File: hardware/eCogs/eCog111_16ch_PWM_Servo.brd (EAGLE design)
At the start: 47.5 x 28 mm, 4 parts

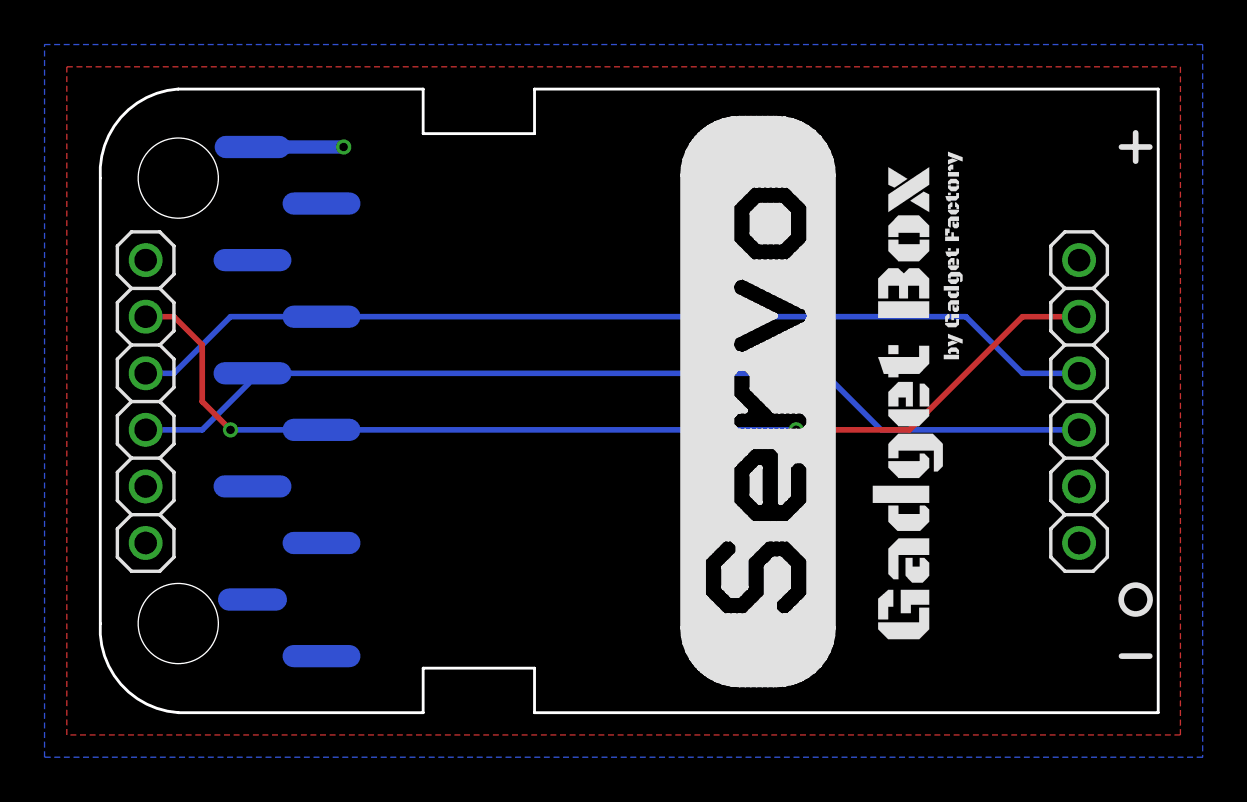
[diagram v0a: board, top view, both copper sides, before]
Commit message: Update eCogs to through hole
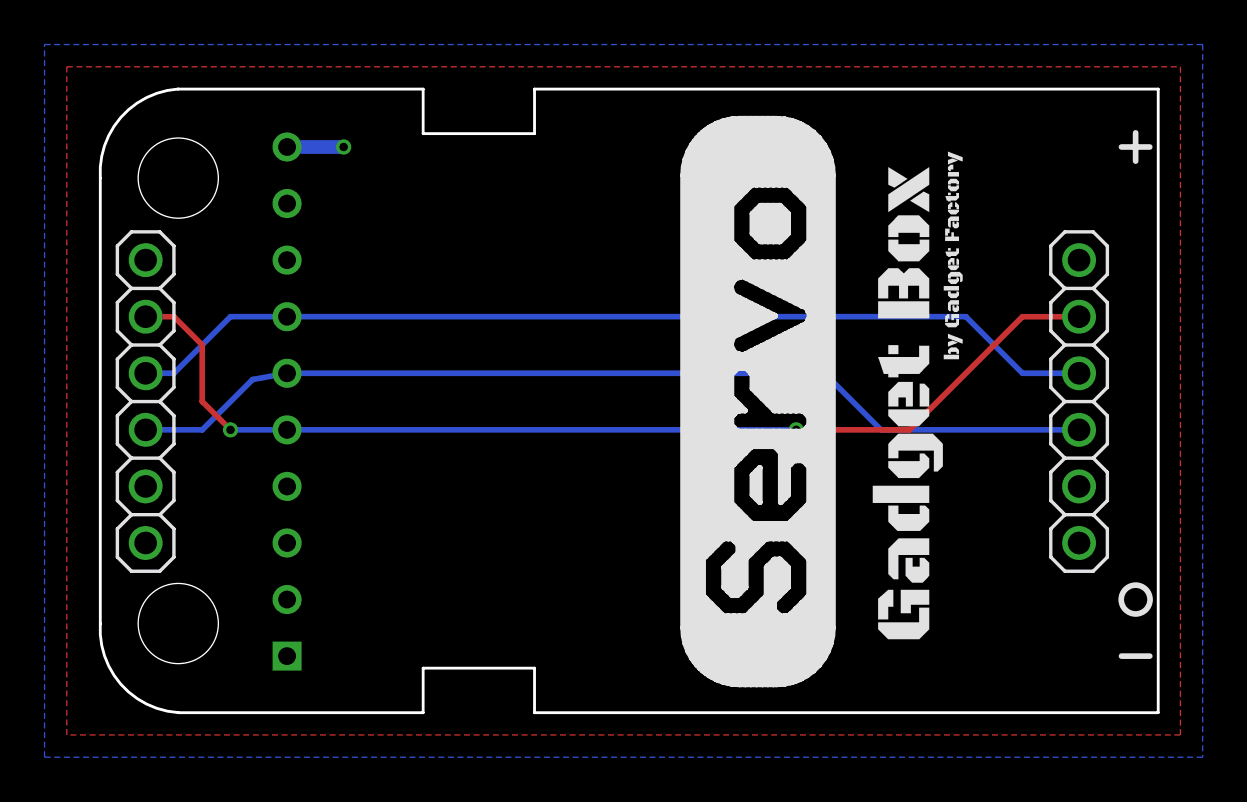
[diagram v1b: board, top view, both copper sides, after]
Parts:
- ECOG: value ECOG_BUSES_ROWECOG_BUSES_SMD -> ECOG_BUSES_ROWTHROUGHHOLE; device eCogs:ECOG_BUSES_SMD -> eCogs:ECOG_BUSES_TH
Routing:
- net 3V3: track 4.09 -> 2.54 mm
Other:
- board text added: "ecog111 v2.1"
- board text removed: "ecog111 v2.0"
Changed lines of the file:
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@@
 <plain>
 <text x="37.559" y="18.415" size="0.8128" layer="22" font="vector" rot="MR0">ecog111.GadgetFactory.net</text>
-<text x="40.702" y="2.159" size="1.016" layer="22" font="vector" rot="MR0">ecog111 v2.0</text>
+<text x="40.702" y="2.159" size="1.016" layer="22" font="vector" rot="MR0">ecog111 v2.1</text>
 <text x="40.702" y="3.429" size="1.016" layer="22" font="vector" rot="MR0">16 Channel PWM/Servo</text>
 <text x="40.702" y="4.699" size="1.016" layer="22" font="vector" rot="MR0">eCogs</text>
@@
 </autorouter>
 <elements>
-<element name="ECOG" library="eCogs" package="ECOG_BUSES_SMD" value="ECOG_BUSES_ROWECOG_BUSES_SMD" x="0" y="0" smashed="yes">
-<attribute name="DIGIKEY" value="S1013EC-10-ND" x="0" y="0" size="1.778" layer="27" display="off"/>
-</element>
+<element name="ECOG" library="eCogs" package="ECOG_BUSES_TH" value="ECOG_BUSES_ROWTHROUGHHOLE" x="0" y="0" smashed="yes"/>
 <element name="JP1" library="GadgetFactory" package="1X06" value="" x="44.45" y="13.97" smashed="yes" rot="R270">
 <attribute name="VALUE" x="41.275" y="21.59" size="1.27" layer="27" rot="R270"/>
@@
 <contactref element="JP1" pad="5"/>
 <contactref element="JP2" pad="5"/>
-<wire x1="7.337490625" y1="25.4" x2="11.43" y2="25.4" width="0.6096" layer="16"/>
+<wire x1="8.89" y1="25.4" x2="11.43" y2="25.4" width="0.6096" layer="16"/>
 <via x="11.43" y="25.4" extent="1-16" drill="0.381"/>
 </signal>
@@
 <contactref element="JP2" pad="2"/>
 <contactref element="ECOG" pad="SPI-CS"/>
-<wire x1="10.436290625" y1="12.7" x2="31.75" y2="12.7" width="0.254" layer="16"/>
+<wire x1="8.89" y1="12.7" x2="31.75" y2="12.7" width="0.254" layer="16"/>
 <via x="31.75" y="12.7" extent="1-16" drill="0.381"/>
 <wire x1="31.75" y1="12.7" x2="36.83" y2="12.7" width="0.254" layer="1"/>
 <wire x1="36.83" y1="12.7" x2="41.91" y2="17.78" width="0.254" layer="1"/>
 <wire x1="41.91" y1="17.78" x2="44.45" y2="17.78" width="0.254" layer="1"/>
-<wire x1="10.436290625" y1="12.7" x2="6.35" y2="12.7" width="0.254" layer="16"/>
+<wire x1="8.89" y1="12.7" x2="6.35" y2="12.7" width="0.254" layer="16"/>
 <via x="6.35" y="12.7" extent="1-16" drill="0.381"/>
 <wire x1="6.35" y1="12.7" x2="5.08" y2="13.97" width="0.254" layer="1"/>
@@
 <contactref element="JP2" pad="3"/>
 <contactref element="ECOG" pad="I2C-SCL"/>
-<wire x1="10.436290625" y1="17.78" x2="39.37" y2="17.78" width="0.254" layer="16"/>
+<wire x1="8.89" y1="17.78" x2="39.37" y2="17.78" width="0.254" layer="16"/>
 <wire x1="39.37" y1="17.78" x2="41.91" y2="15.24" width="0.254" layer="16"/>
 <wire x1="41.91" y1="15.24" x2="44.45" y2="15.24" width="0.254" layer="16"/>
-<wire x1="10.436290625" y1="17.78" x2="6.35" y2="17.78" width="0.254" layer="16"/>
+<wire x1="8.89" y1="17.78" x2="6.35" y2="17.78" width="0.254" layer="16"/>
 <wire x1="6.35" y1="17.78" x2="3.81" y2="15.24" width="0.254" layer="16"/>
 <wire x1="3.81" y1="15.24" x2="2.54" y2="15.24" width="0.254" layer="16"/>
@@
 <contactref element="JP2" pad="4"/>
 <contactref element="ECOG" pad="I2C-SDA"/>
-<wire x1="7.337490625" y1="15.24" x2="33.02" y2="15.24" width="0.254" layer="16"/>
+<wire x1="8.89" y1="15.24" x2="33.02" y2="15.24" width="0.254" layer="16"/>
 <wire x1="33.02" y1="15.24" x2="35.56" y2="12.7" width="0.254" layer="16"/>
 <wire x1="35.56" y1="12.7" x2="44.45" y2="12.7" width="0.254" layer="16"/>
-<wire x1="7.337490625" y1="15.24" x2="7.337490625" y2="14.957490625" width="0.254" layer="16"/>
+<wire x1="8.89" y1="15.24" x2="7.337490625" y2="14.957490625" width="0.254" layer="16"/>
 <wire x1="7.337490625" y1="14.957490625" x2="5.08" y2="12.7" width="0.254" layer="16"/>
 <wire x1="5.08" y1="12.7" x2="2.54" y2="12.7" width="0.254" layer="16"/>
